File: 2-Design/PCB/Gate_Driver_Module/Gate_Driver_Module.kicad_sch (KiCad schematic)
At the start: 10 parts, among them J1 Conn_01x04_Male, J2 Conn_01x04_Male, U1 ROE-0512S, U2 LTV-817, U3 TC4421A

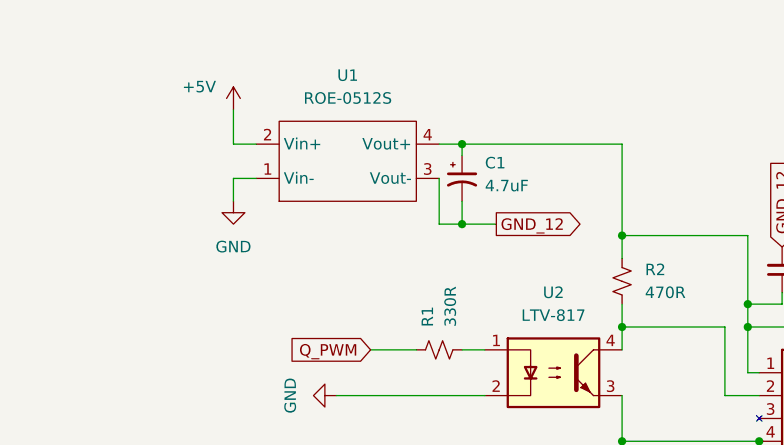
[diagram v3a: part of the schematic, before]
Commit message: Gate Driver Module minimum load for boost, plus Controller Module advancements
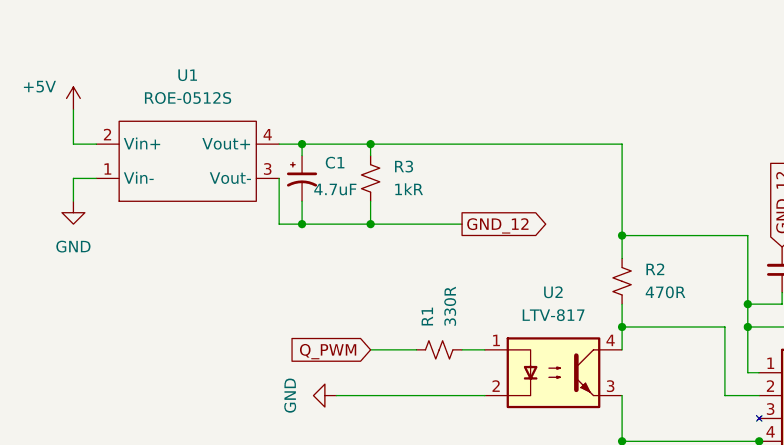
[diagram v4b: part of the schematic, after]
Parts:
- added R3: 1kR, Resistor_SMD:R_0805_2012Metric_Pad1.20x1.40mm_HandSolder, symbol Device:R_Small_US
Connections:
- net GND_12: now also R3.1
- net at C1.1, C2.1, C3.1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: now also R3.2
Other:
- moved on the sheet: C1, U1
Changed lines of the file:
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@@
   (junction (at 130.81 95.25) (diameter 0) (color 0 0 0 0)
   )
-  (junction (at 97.79 71.12) (diameter 0) (color 0 0 0 0)
-  )
-  (junction (at 97.79 62.23) (diameter 0) (color 0 0 0 0)
+  (junction (at 87.63 71.12) (diameter 0) (color 0 0 0 0)
+  )
+  (junction (at 80.01 71.12) (diameter 0) (color 0 0 0 0)
+  )
+  (junction (at 87.63 62.23) (diameter 0) (color 0 0 0 0)
+  )
+  (junction (at 80.01 62.23) (diameter 0) (color 0 0 0 0)
   )
   (junction (at 115.57 95.25) (diameter 0) (color 0 0 0 0)
@@
     (stroke (width 0) (type default) (color 0 0 0 0))
   )
-  (wire (pts (xy 72.39 62.23) (xy 74.93 62.23))
+  (wire (pts (xy 54.61 62.23) (xy 57.15 62.23))
     (stroke (width 0) (type default) (color 0 0 0 0))
   )
@@
     (stroke (width 0) (type default) (color 0 0 0 0))
   )
+  (wire (pts (xy 87.63 63.5) (xy 87.63 62.23))
+    (stroke (width 0) (type default) (color 0 0 0 0))
+  )
   (wire (pts (xy 129.54 80.01) (xy 133.35 80.01))
     (stroke (width 0) (type default) (color 0 0 0 0))
   )
-  (wire (pts (xy 72.39 66.04) (xy 74.93 66.04))
+  (wire (pts (xy 54.61 66.04) (xy 57.15 66.04))
     (stroke (width 0) (type default) (color 0 0 0 0))
   )
@@
     (stroke (width 0) (type default) (color 0 0 0 0))
   )
-  (wire (pts (xy 97.79 62.23) (xy 97.79 63.5))
+  (wire (pts (xy 80.01 62.23) (xy 80.01 63.5))
+    (stroke (width 0) (type default) (color 0 0 0 0))
+  )
+  (wire (pts (xy 87.63 71.12) (xy 97.79 71.12))
     (stroke (width 0) (type default) (color 0 0 0 0))
   )
@@
     (stroke (width 0) (type default) (color 0 0 0 0))
   )
-  (wire (pts (xy 72.39 58.42) (xy 72.39 62.23))
+  (wire (pts (xy 54.61 58.42) (xy 54.61 62.23))
     (stroke (width 0) (type default) (color 0 0 0 0))
   )
@@
     (stroke (width 0) (type default) (color 0 0 0 0))
   )
-  (wire (pts (xy 72.39 66.04) (xy 72.39 68.58))
+  (wire (pts (xy 54.61 66.04) (xy 54.61 68.58))
     (stroke (width 0) (type default) (color 0 0 0 0))
   )
@@
     (stroke (width 0) (type default) (color 0 0 0 0))
   )
+  (wire (pts (xy 87.63 62.23) (xy 80.01 62.23))
+    (stroke (width 0) (type default) (color 0 0 0 0))
+  )
   (wire (pts (xy 151.13 95.25) (xy 154.94 95.25))
     (stroke (width 0) (type default) (color 0 0 0 0))
@@
     (stroke (width 0) (type default) (color 0 0 0 0))
   )
-  (wire (pts (xy 97.79 68.58) (xy 97.79 71.12))
-    (stroke (width 0) (type default) (color 0 0 0 0))
-  )
-  (wire (pts (xy 95.25 62.23) (xy 97.79 62.23))
+  (wire (pts (xy 80.01 68.58) (xy 80.01 71.12))
+    (stroke (width 0) (type default) (color 0 0 0 0))
+  )
+  (wire (pts (xy 77.47 62.23) (xy 80.01 62.23))
     (stroke (width 0) (type default) (color 0 0 0 0))
   )
@@
     (stroke (width 0) (type default) (color 0 0 0 0))
   )
-  (wire (pts (xy 95.25 71.12) (xy 97.79 71.12))
+  (wire (pts (xy 77.47 71.12) (xy 80.01 71.12))
     (stroke (width 0) (type default) (color 0 0 0 0))
   )
@@
     (stroke (width 0) (type default) (color 0 0 0 0))
   )
+  (wire (pts (xy 87.63 68.58) (xy 87.63 71.12))
+    (stroke (width 0) (type default) (color 0 0 0 0))
+  )
   (wire (pts (xy 97.79 85.09) (xy 100.33 85.09))
     (stroke (width 0) (type default) (color 0 0 0 0))
@@
     (stroke (width 0) (type default) (color 0 0 0 0))
   )
-  (wire (pts (xy 95.25 71.12) (xy 95.25 66.04))
+  (wire (pts (xy 77.47 71.12) (xy 77.47 66.04))
     (stroke (width 0) (type default) (color 0 0 0 0))
   )
@@
     (stroke (width 0) (type default) (color 0 0 0 0))
   )
-  (wire (pts (xy 115.57 62.23) (xy 97.79 62.23))
+  (wire (pts (xy 115.57 62.23) (xy 87.63 62.23))
     (stroke (width 0) (type default) (color 0 0 0 0))
   )
@@
     (stroke (width 0) (type default) (color 0 0 0 0))
   )
-  (wire (pts (xy 97.79 71.12) (xy 101.6 71.12))
+  (wire (pts (xy 80.01 71.12) (xy 87.63 71.12))
     (stroke (width 0) (type default) (color 0 0 0 0))
   )
@@
     )
   )
-  (global_label "GND_12" (shape output) (at 101.6 71.12 0) (fields_autoplaced)
-    (effects (font (size 1.27 1.27)) (justify left))
-    (property "Intersheet References" "${INTERSHEET_REFS}" (id 0) (at 111.2702 71.1994 0)
+  (global_label "GND_12" (shape output) (at 97.79 71.12 0) (fields_autoplaced)
+    (effects (font (size 1.27 1.27)) (justify left))
+    (property "Intersheet References" "${INTERSHEET_REFS}" (id 0) (at 107.4602 71.1994 0)
       (effects (font (size 1.27 1.27)) (justify left) hide)
     )
@@
   )
   (symbol (lib_id "Device:R_Small_US") (at 95.25 85.09 270) (unit 1)
-    (in_bom yes) (on_board yes) (fields_autoplaced)
+    (in_bom yes) (on_board yes)
     (property "Reference" "R1" (id 0) (at 93.9799 82.55 0)
       (effects (font (size 1.27 1.27)) (justify right))
@@
     (pin "2")
   )
-  (symbol (lib_id "ee463_symbol_library:ROE-0512S") (at 85.09 64.77 0) (mirror x) (unit 1)
-    (in_bom yes) (on_board yes) (fields_autoplaced)
-    (property "Reference" "U1" (id 0) (at 85.09 54.61 0))
-    (property "Value" "ROE-0512S" (id 1) (at 85.09 57.15 0))
-    (property "Footprint" "ee463_footprint_lib:ROE-0512S" (id 2) (at 85.09 64.77 0)
-      (effects (font (size 1.27 1.27)) hide)
-    )
-    (property "Datasheet" "" (id 3) (at 85.09 64.77 0)
+  (symbol (lib_id "ee463_symbol_library:ROE-0512S") (at 67.31 64.77 0) (mirror x) (unit 1)
+    (in_bom yes) (on_board yes) (fields_autoplaced)
+    (property "Reference" "U1" (id 0) (at 67.31 54.61 0))
+    (property "Value" "ROE-0512S" (id 1) (at 67.31 57.15 0))
+    (property "Footprint" "ee463_footprint_lib:ROE-0512S" (id 2) (at 67.31 64.77 0)
+      (effects (font (size 1.27 1.27)) hide)
+    )
+    (property "Datasheet" "" (id 3) (at 67.31 64.77 0)
       (effects (font (size 1.27 1.27)) hide)
     )
@@
     (pin "4")
   )
+  (symbol (lib_id "Device:R_Small_US") (at 87.63 66.04 180) (unit 1)
+    (in_bom yes) (on_board yes) (fields_autoplaced)
+    (property "Reference" "R3" (id 0) (at 90.17 64.7699 0)
+      (effects (font (size 1.27 1.27)) (justify right))
+    )
+    (property "Value" "1kR" (id 1) (at 90.17 67.3099 0)
+      (effects (font (size 1.27 1.27)) (justify right))
+    )
+    (property "Footprint" "Resistor_SMD:R_0805_2012Metric_Pad1.20x1.40mm_HandSolder" (id 2) (at 87.63 66.04 0)
+      (effects (font (size 1.27 1.27)) hide)
+    )
+    (property "Datasheet" "~" (id 3) (at 87.63 66.04 0)
+      (effects (font (size 1.27 1.27)) hide)
+    )
+    (pin "1")
+    (pin "2")
+  )
   (symbol (lib_id "Device:C_Small") (at 149.86 76.2 0) (mirror x) (unit 1)
     (in_bom yes) (on_board yes) (fields_autoplaced)
@@
     (pin "2")
   )
-  (symbol (lib_id "Device:C_Polarized_Small_US") (at 97.79 66.04 0) (unit 1)
-    (in_bom yes) (on_board yes) (fields_autoplaced)
-    (property "Reference" "C1" (id 0) (at 100.33 64.3381 0)
+  (symbol (lib_id "Device:C_Polarized_Small_US") (at 80.01 66.04 0) (unit 1)
+    (in_bom yes) (on_board yes)
+    (property "Reference" "C1" (id 0) (at 82.55 64.3381 0)
       (effects (font (size 1.27 1.27)) (justify left))
     )
-    (property "Value" "4.7uF" (id 1) (at 100.33 66.8781 0)
+    (property "Value" "4.7uF" (id 1) (at 81.28 67.31 0)
       (effects (font (size 1.27 1.27)) (justify left))
     )
-    (property "Footprint" "Capacitor_SMD:CP_Elec_4x5.4" (id 2) (at 97.79 66.04 0)
-      (effects (font (size 1.27 1.27)) hide)
-    )
-    (property "Datasheet" "~" (id 3) (at 97.79 66.04 0)
+    (property "Footprint" "Capacitor_SMD:CP_Elec_4x5.4" (id 2) (at 80.01 66.04 0)
+      (effects (font (size 1.27 1.27)) hide)
+    )
+    (property "Datasheet" "~" (id 3) (at 80.01 66.04 0)
       (effects (font (size 1.27 1.27)) hide)
     )
@@
     (pin "4")
   )
-  (symbol (lib_id "power:+5V") (at 72.39 58.42 0) (unit 1)
+  (symbol (lib_id "power:+5V") (at 54.61 58.42 0) (unit 1)
     (in_bom yes) (on_board yes)
-    (property "Reference" "#PWR0102" (id 0) (at 72.39 62.23 0)
-      (effects (font (size 1.27 1.27)) hide)
-    )
-    (property "Value" "+5V" (id 1) (at 68.58 55.88 0))
-    (property "Footprint" "" (id 2) (at 72.39 58.42 0)
-      (effects (font (size 1.27 1.27)) hide)
-    )
-    (property "Datasheet" "" (id 3) (at 72.39 58.42 0)
+    (property "Reference" "#PWR0102" (id 0) (at 54.61 62.23 0)
+      (effects (font (size 1.27 1.27)) hide)
+    )
+    (property "Value" "+5V" (id 1) (at 50.8 55.88 0))
+    (property "Footprint" "" (id 2) (at 54.61 58.42 0)
+      (effects (font (size 1.27 1.27)) hide)
+    )
+    (property "Datasheet" "" (id 3) (at 54.61 58.42 0)
       (effects (font (size 1.27 1.27)) hide)
     )
@@
     (pin "8")
   )
-  (symbol (lib_id "power:GND") (at 72.39 68.58 0) (unit 1)
-    (in_bom yes) (on_board yes) (fields_autoplaced)
-    (property "Reference" "#PWR0103" (id 0) (at 72.39 74.93 0)
-      (effects (font (size 1.27 1.27)) hide)
-    )
-    (property "Value" "GND" (id 1) (at 72.39 73.66 0))
-    (property "Footprint" "" (id 2) (at 72.39 68.58 0)
-      (effects (font (size 1.27 1.27)) hide)
-    )
-    (property "Datasheet" "" (id 3) (at 72.39 68.58 0)
+  (symbol (lib_id "power:GND") (at 54.61 68.58 0) (unit 1)
+    (in_bom yes) (on_board yes) (fields_autoplaced)
+    (property "Reference" "#PWR0103" (id 0) (at 54.61 74.93 0)
+      (effects (font (size 1.27 1.27)) hide)
+    )
+    (property "Value" "GND" (id 1) (at 54.61 73.66 0))
+    (property "Footprint" "" (id 2) (at 54.61 68.58 0)
+      (effects (font (size 1.27 1.27)) hide)
+    )
+    (property "Datasheet" "" (id 3) (at 54.61 68.58 0)
       (effects (font (size 1.27 1.27)) hide)
     )
@@
       (reference "R2") (unit 1) (value "470R") (footprint "Resistor_SMD:R_0805_2012Metric_Pad1.20x1.40mm_HandSolder")
     )
+    (path "/58e27867-0734-4ab3-93d8-ebb346a967a5"
+      (reference "R3") (unit 1) (value "1kR") (footprint "Resistor_SMD:R_0805_2012Metric_Pad1.20x1.40mm_HandSolder")
+    )
     (path "/33cdb0cc-6d22-4743-9958-cf0e61104689"

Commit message: Some changes i dont even remember
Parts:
- R1: value 330R -> 470-330-220-100R
- R2: value 470R -> 680-470-330-220R
- R3: value 1kR -> 1kR, 0.25W
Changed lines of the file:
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@@
       (effects (font (size 1.27 1.27)) (justify right))
     )
-    (property "Value" "330R" (id 1) (at 96.5199 82.55 0)
+    (property "Value" "470-330-220-100R" (id 1) (at 96.5199 82.55 0)
       (effects (font (size 1.27 1.27)) (justify right))
     )
@@
   )
   (symbol (lib_id "Device:R_Small_US") (at 115.57 77.47 180) (unit 1)
-    (in_bom yes) (on_board yes) (fields_autoplaced)
-    (property "Reference" "R2" (id 0) (at 118.11 76.1999 0)
-      (effects (font (size 1.27 1.27)) (justify right))
-    )
-    (property "Value" "470R" (id 1) (at 118.11 78.7399 0)
+    (in_bom yes) (on_board yes)
+    (property "Reference" "R2" (id 0) (at 118.11 76.2 0)
+      (effects (font (size 1.27 1.27)) (justify right))
+    )
+    (property "Value" "680-470-330-220R" (id 1) (at 110.49 78.74 0)
       (effects (font (size 1.27 1.27)) (justify right))
     )
@@
       (effects (font (size 1.27 1.27)) (justify right))
     )
-    (property "Value" "1kR" (id 1) (at 90.17 67.3099 0)
+    (property "Value" "1kR, 0.25W" (id 1) (at 90.17 67.3099 0)
       (effects (font (size 1.27 1.27)) (justify right))
     )
@@
     )
     (path "/18a5f8d6-a2fb-43cb-bab5-732d0df75ee1"
-      (reference "R1") (unit 1) (value "330R") (footprint "Resistor_SMD:R_0805_2012Metric_Pad1.20x1.40mm_HandSolder")
+      (reference "R1") (unit 1) (value "470-330-220-100R") (footprint "Resistor_SMD:R_0805_2012Metric_Pad1.20x1.40mm_HandSolder")
     )
     (path "/2418fc4e-2563-4153-a48d-fbafff8c28a6"
-      (reference "R2") (unit 1) (value "470R") (footprint "Resistor_SMD:R_0805_2012Metric_Pad1.20x1.40mm_HandSolder")
+      (reference "R2") (unit 1) (value "680-470-330-220R") (footprint "Resistor_SMD:R_0805_2012Metric_Pad1.20x1.40mm_HandSolder")
     )
     (path "/58e27867-0734-4ab3-93d8-ebb346a967a5"
-      (reference "R3") (unit 1) (value "1kR") (footprint "Resistor_SMD:R_0805_2012Metric_Pad1.20x1.40mm_HandSolder")
+      (reference "R3") (unit 1) (value "1kR, 0.25W") (footprint "Resistor_SMD:R_0805_2012Metric_Pad1.20x1.40mm_HandSolder")
     )
     (path "/33cdb0cc-6d22-4743-9958-cf0e61104689"
